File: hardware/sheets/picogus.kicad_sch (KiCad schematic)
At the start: 59 parts, among them J1 DMA_JP, J5 SWD, SW1 BOOTSEL, U1 RP2040, U10 74LVC2G06, U11 APS6404L, U12 PCM5102A, U2 W25Q128JVS, U3 AMS1117-3.3, U4 CB3T3257, U5 CB3T3257, U6 CB3T3245, U7 74AHC14, U8 74LVC00, U9 74LVC00, Y1 12MHz

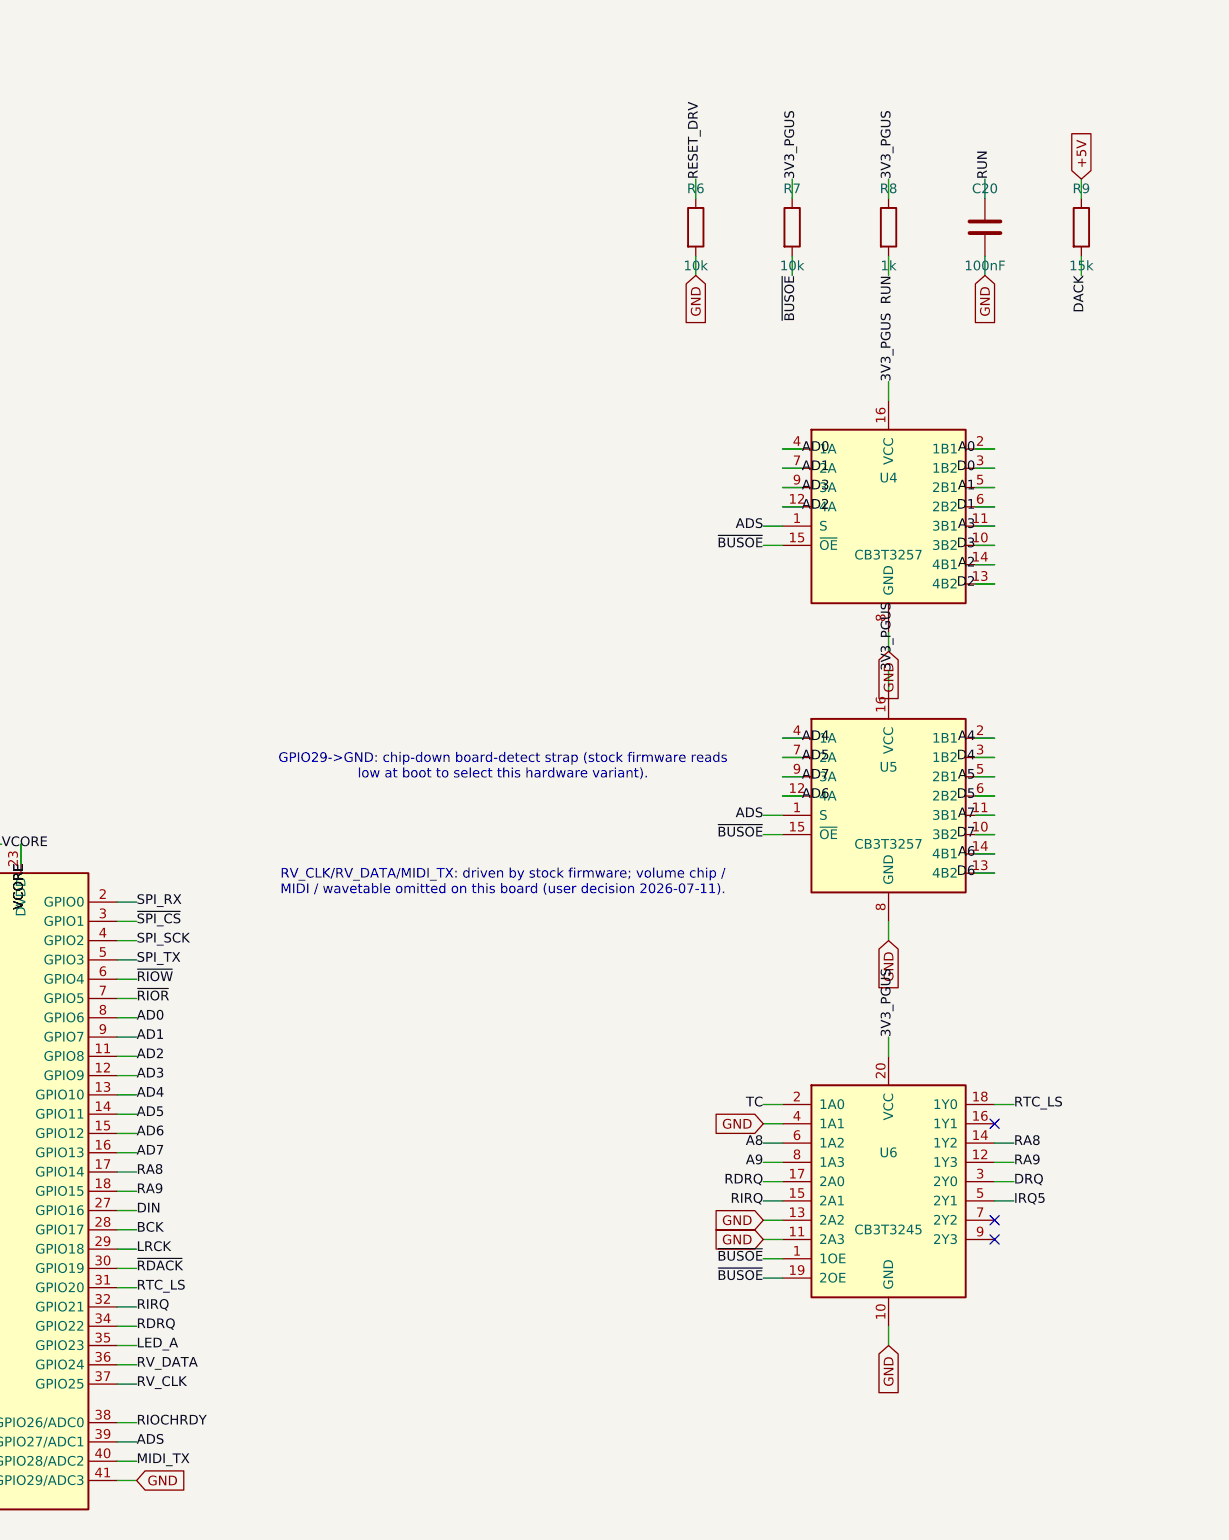
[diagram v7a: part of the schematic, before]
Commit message: video/picogus/audio: MCUs direct on 3.3V bus, shifters deleted
video.py: deleted U6 (control snoop) and U7 (IOCHRDY driver) -- pure
fixed-direction 74LVC245A buffers with nothing left to do once the ISA
bus is 3.3V-native. GPIO8-11/20/21/38/39 now label directly onto
~{MEMR}/~{MEMW}/~{IOR}/~{IOW}/BALE/AEN/CLK/RESET_DRV; GPIO27 drives
IOCHRDY directly (native tri-state); GPIO40 freed. Kept U2-U5: they are
a GPIO-budget time-division mux sharing one 8-bit snoop bus across
D0-7/A0-19, not a voltage bridge -- deleting them would need 28 GPIO
this 48-pin part doesn't have (questions-video.md #10).

picogus.py: deleted U6 (CB3T3245) -- pure fixed-direction buffering
for A8/A9/TC/IRQ5/DRQ with no muxing role; GPIO17/18/31/32/34 now
direct on those nets (gpio_map updated, mapping table preserved exactly
per 3v3-verification.md check 6). Kept U4/U5 (CB3T3257 GPIO-budget
mux) and U7/U8/U9/U10 (real Schmitt/NAND/latch/open-drain logic, never
level shifters -- already ran on 3V3_PGUS). Also fixed R9's DACK
pull-up from +5V to 3V3_PGUS: it fed 3.3V-domain gate inputs one hop
from RP2040 GPIO6/7 and had no business parking at 5V post-redesign.

audio.py: no shifter exists on this sheet (grep LVC matches only a
comment) -- pure analog summer, nothing to change. Logged as a no-op
finding.

Validated each sheet (zero structural ERC); full build exits 0.

Co-Authored-By: Claude Fable 5 <noreply@anthropic.com>
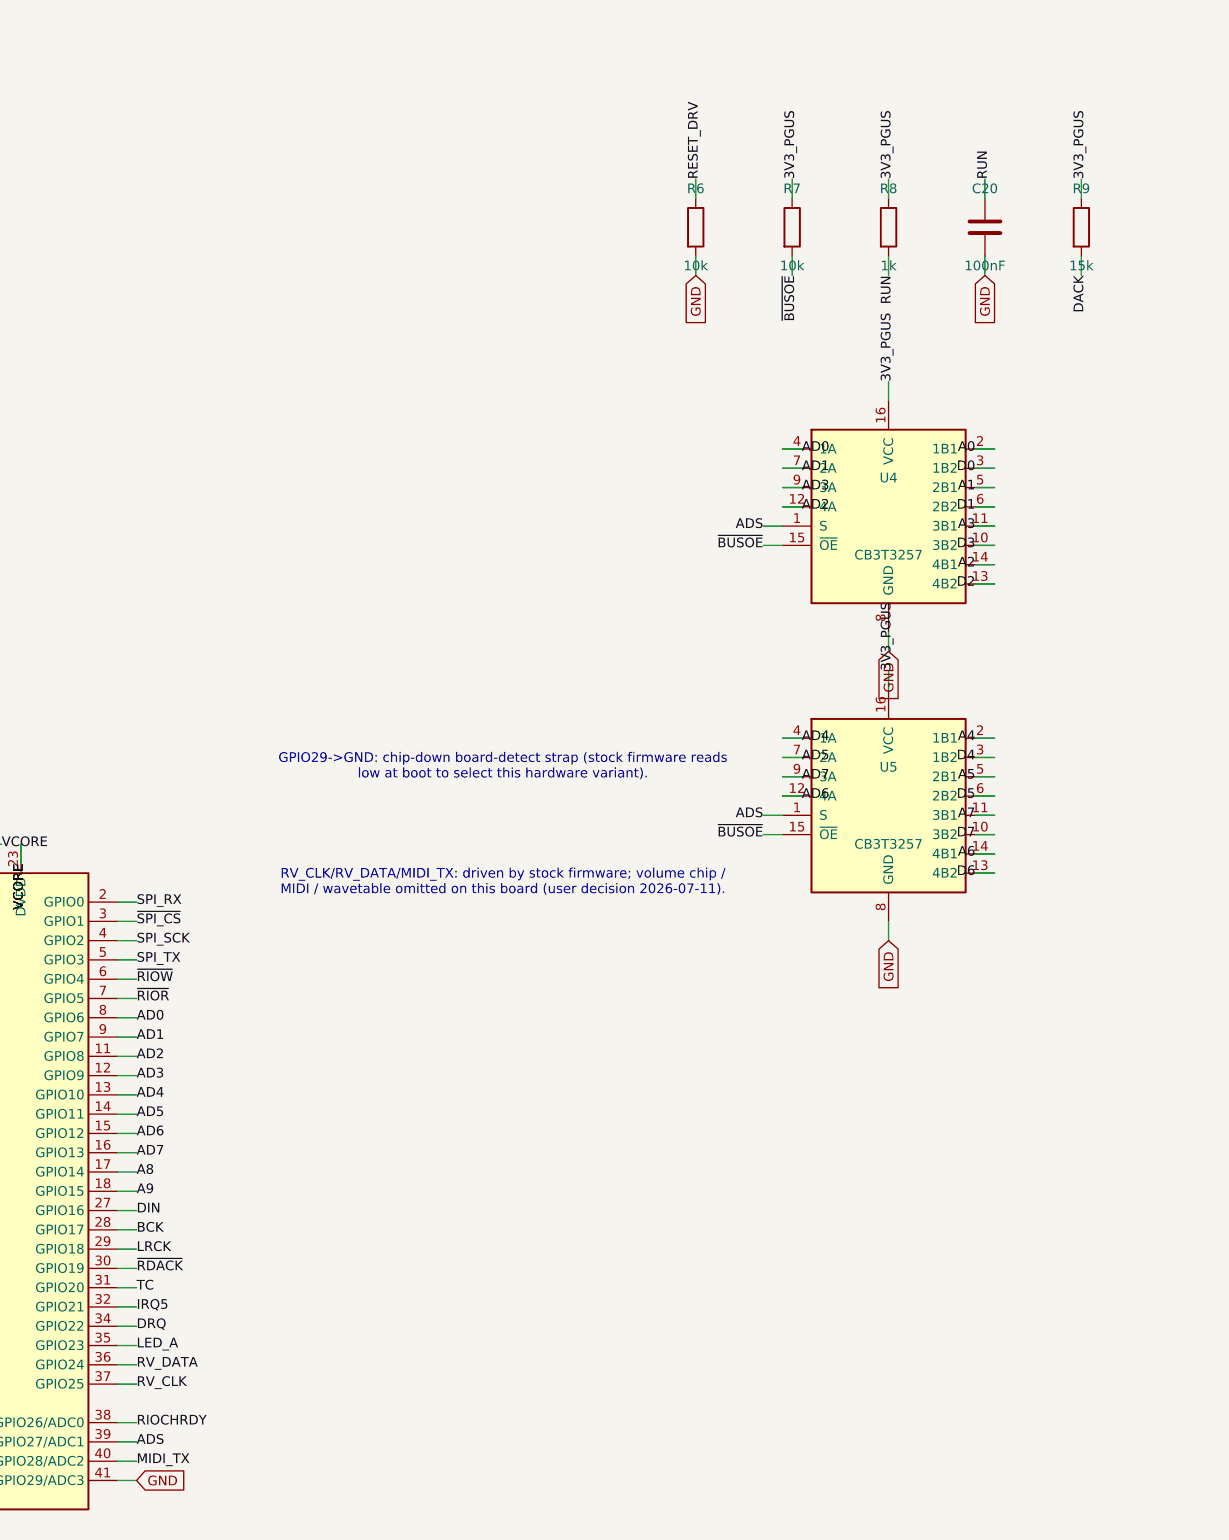
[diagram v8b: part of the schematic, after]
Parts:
- removed J1: DMA_JP, Connector_PinHeader_2.54mm:PinHeader_2x04_P2.54mm_Vertical, symbol Connector_Generic:Conn_02x04_Odd_Even
- removed U7: 74AHC14, Package_SO:TSSOP-14_4.4x5mm_P0.65mm, symbol mini-xt:74HCT04
- added U10: 74LVC2G06, Package_TO_SOT_SMD:SOT-23-6, symbol mini-xt:74LVC2G06
- J1: renamed from U10; value 74LVC2G06 -> DMA_JP; footprint Package_TO_SOT_SMD:SOT-23-6 -> Connector_PinHeader_2.54mm:PinHeader_2x04_P2.54mm_Vertical; symbol mini-xt:74LVC2G06 -> Connector_Generic:Conn_02x04_Odd_Even; LCSC Part Num C52145914 -> C2333
- U7: renamed from U6; value CB3T3245 -> 74AHC14; footprint Package_SO:TSSOP-20_4.4x6.5mm_P0.65mm -> Package_SO:TSSOP-14_4.4x5mm_P0.65mm; symbol mini-xt:CB3T3245 -> mini-xt:74HCT04; LCSC Part Num C15298 -> C54561786
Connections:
- net +5V: no longer R9.1
- net 3V3_PGUS: now also R9.1, U7.14 (VCC), U10.5 (VCC); no longer J1.5 (VCC), U7.20 (VCC)
- net A8: now also U1.17 (GPIO14); no longer U7.6 (1A2)
- net A9: now also U1.18 (GPIO15); no longer U7.8 (1A3)
- net ADS: now also U7.13 (P13)
- net ADS_INV: now also U7.12 (P12)
- net DACK: now also J1.4 (Pin_4), J1.8 (Pin_8), U7.5 (P5)
- net DRQ: now also J1.2 (Pin_2), J1.6 (Pin_6), U1.34 (GPIO22); no longer U7.3 (2Y0)
- net DRQ1: now also J1.1 (Pin_1)
- net DRQ3: now also J1.5 (Pin_5)
- net GND: now also U7.7 (GND), U10.2 (GND), U10.3 (2A); no longer J1.2 (GND), J1.3 (2A), U7.10 (GND), U7.11 (2A3), U7.13 (2A2), U7.4 (1A1)
- net IOCHRDY: now also U10.6 (1Y); no longer J1.6 (1Y)
- net IOR_POS: now also U7.2 (P2)
- net IOW_POS: now also U7.4 (P4)
- net IRQ5: now also U1.32 (GPIO21); no longer U7.5 (2Y1)
- net RESET_DRV: now also U7.11 (P11)
- net RIOCHRDY: now also U10.1 (1A); no longer J1.1 (1A)
- net RST_DLY: now also U7.8 (P8)
- net RST_INV: now also U7.10 (P10), U7.9 (P9)
- net TC: now also U1.31 (GPIO20); no longer U7.2 (1A0)
- net ~{BUSOE}: no longer U7.1 (1OE), U7.19 (2OE)
- net ~{DACK1}: now also J1.3 (Pin_3)
- net ~{DACK3}: now also J1.7 (Pin_7)
- net ~{IOR}: now also U7.1 (P1)
- net ~{IOW}: now also U7.3 (P3)
- net ~{RDACK}: now also U7.6 (P6)
- removed net RA8: U1.17 (GPIO14), U7.14 (1Y2)
- removed net RA9: U1.18 (GPIO15), U7.12 (1Y3)
- removed net RDRQ: U1.34 (GPIO22), U7.17 (2A0)
- removed net RIRQ: U1.32 (GPIO21), U7.15 (2A1)
- removed net RTC_LS: U1.31 (GPIO20), U7.18 (1Y0)
- no-connect marks 8 -> 5
